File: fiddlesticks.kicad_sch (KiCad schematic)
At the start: 57 parts, among them J1 USB_C_Receptacle_USB2.0_16P, J2 Conn_01x04_Pin, J3 Conn_02x04_Counter_Clockwise, J4 Conn_01x04_Socket, M1 Motor_DC, M2 Motor_DC, M3 Motor_DC, M4 Motor_DC, Q1 AO3400A, Q2 AO3400A, Q3 AO3400A, Q4 AO3400A, SW1 SW_Push, SW2 SW_SPDT, U1 STM32F411CEUx, U2 USBLC6-2SC6, U3 ICM-45605, U4 SPX3819M5-L-3-3, Y1 8MHz 18pF

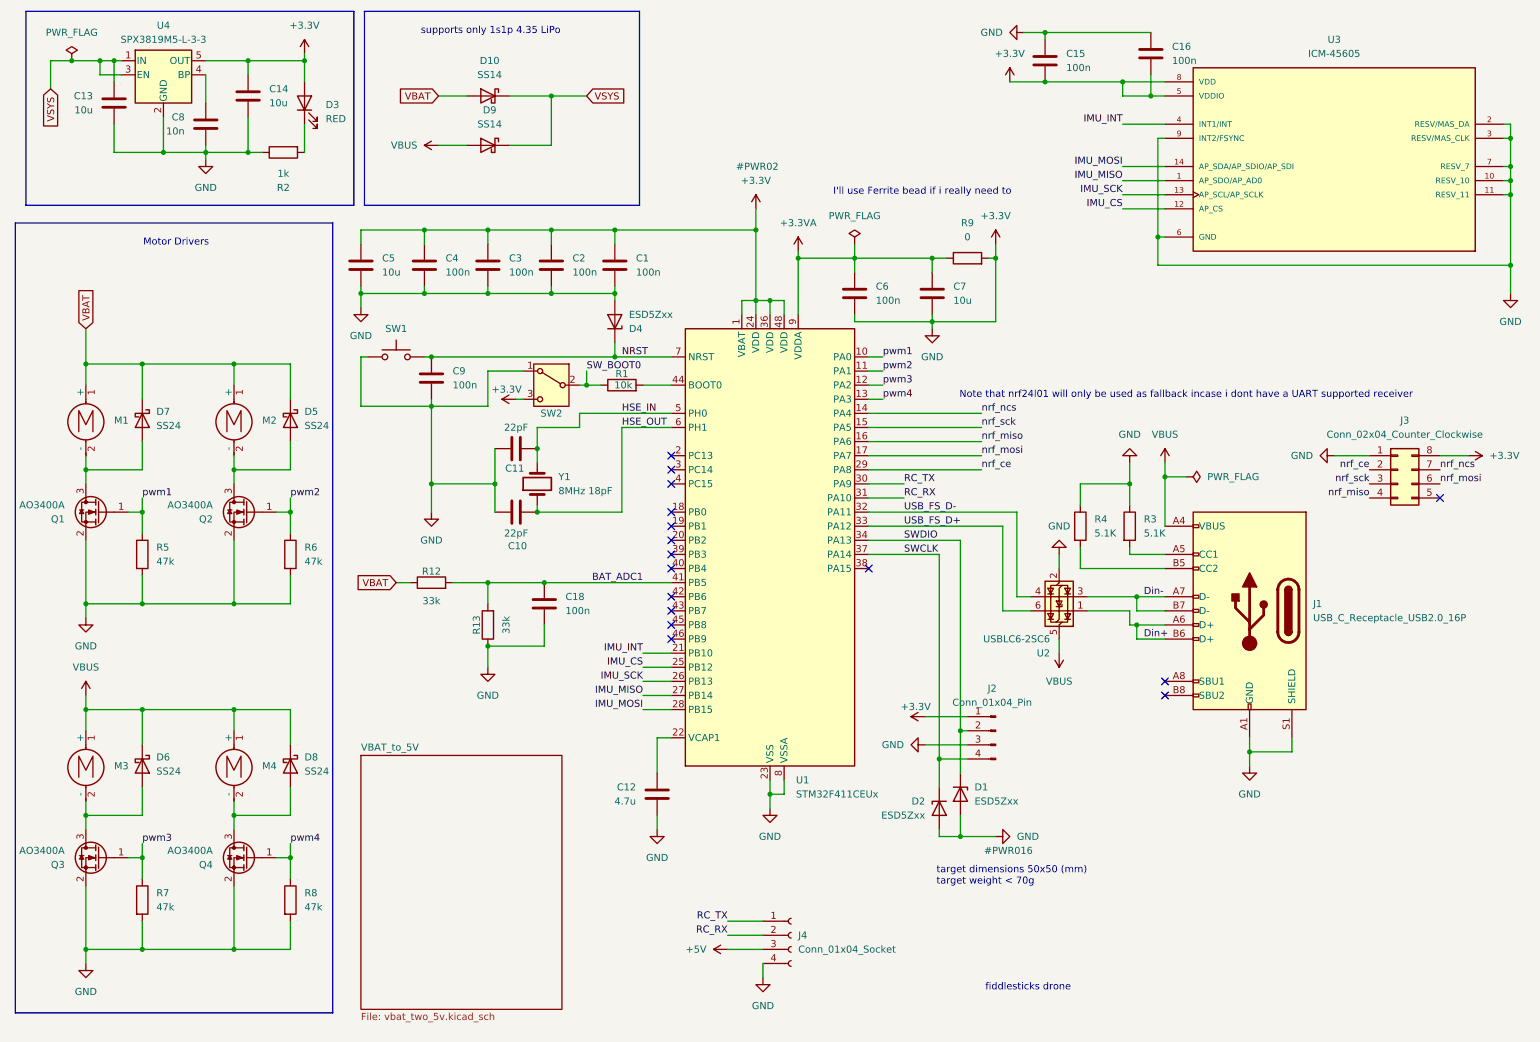
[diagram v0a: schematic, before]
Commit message: changed diodes for power ORing
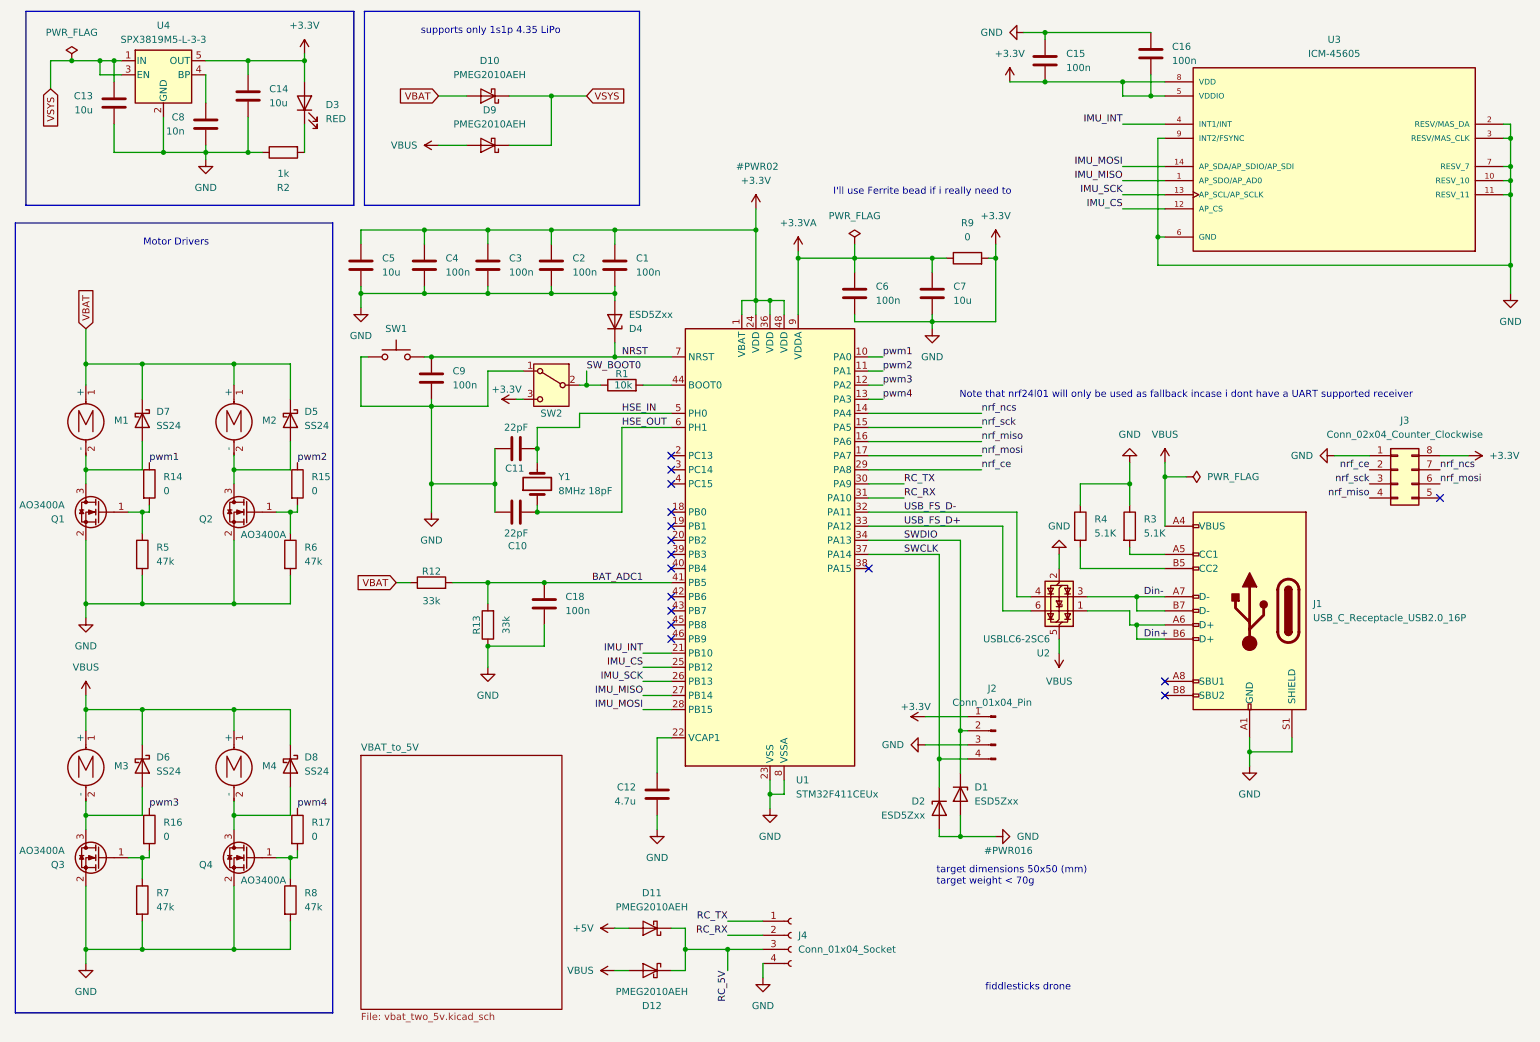
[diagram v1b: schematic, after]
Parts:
- removed D10, D9: SS14, Diode_SMD:D_SMA, symbol Diode:SS14
- added D10, D11, D12, D9: PMEG2010AEH, Diode_SMD:D_SOD-123F, symbol Diode:PMEG2010AEH
- added R14, R15, R16, R17: 0, symbol Device:R
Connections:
- net +5V: now also D11.2 (A); no longer J4.3 (Pin_3)
- net VBAT: now also D10.2 (A)
- net VBUS: now also D12.2 (A), D9.2 (A)
- net VSYS: now also D10.1 (K), D9.1 (K)
- net pwm1: now also R14.1; no longer Q1.1 (G), R5.1
- net pwm2: now also R15.1; no longer Q2.1 (G), R6.1
- net pwm3: now also R16.1; no longer Q3.1 (G), R7.1
- net pwm4: now also R17.1; no longer Q4.1 (G), R8.1
- new net: Q3.1 (G), R16.2, R7.1
- new net: Q1.1 (G), R14.2, R5.1
- new net: Q2.1 (G), R15.2, R6.1
- new net: Q4.1 (G), R17.2, R8.1
- new net RC_5V: D11.1 (K), D12.1 (K), J4.3 (Pin_3)

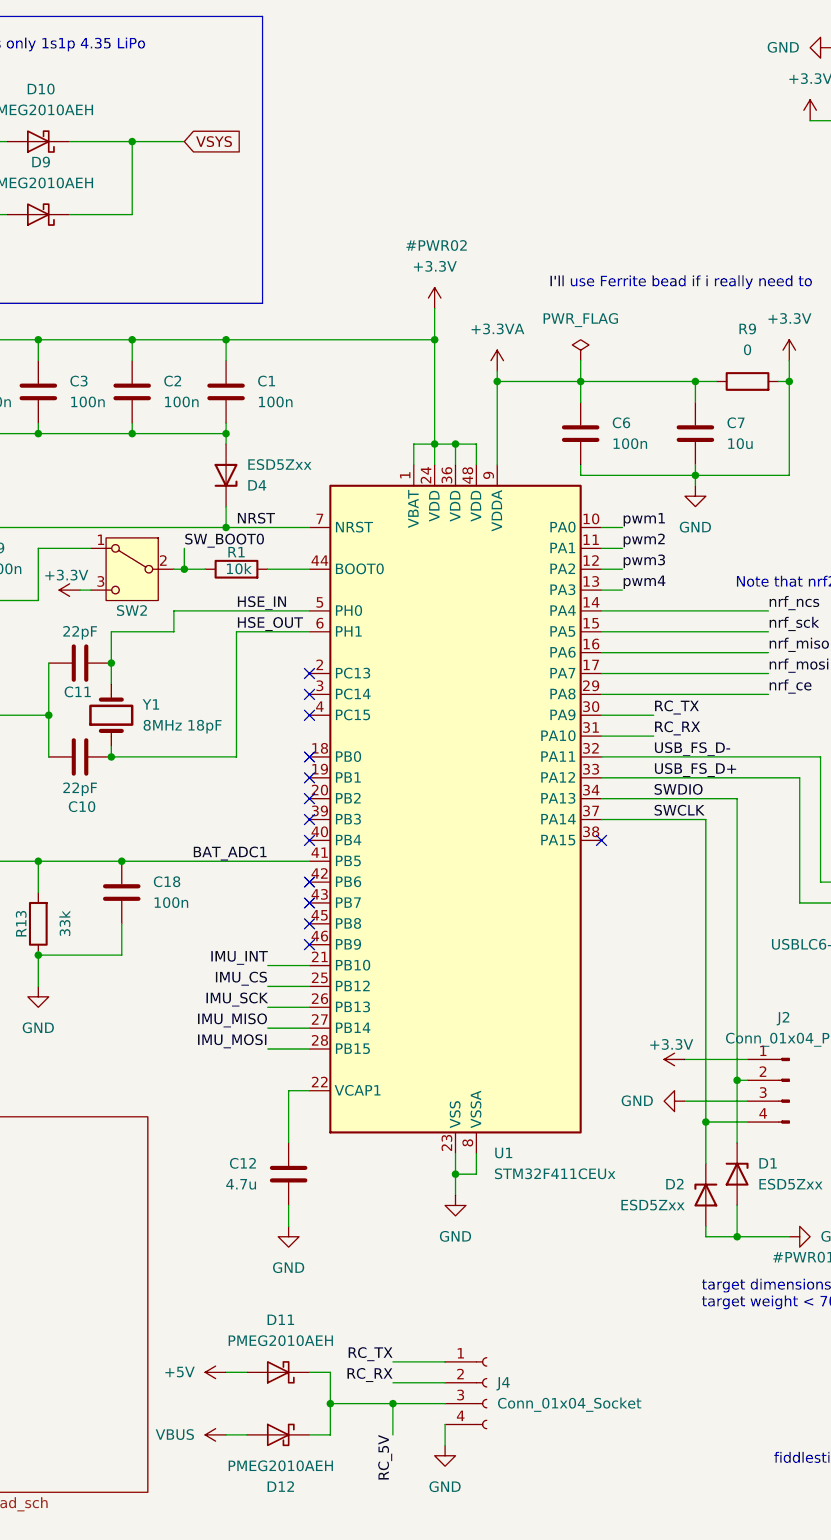
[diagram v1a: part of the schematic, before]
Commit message: added battery connector
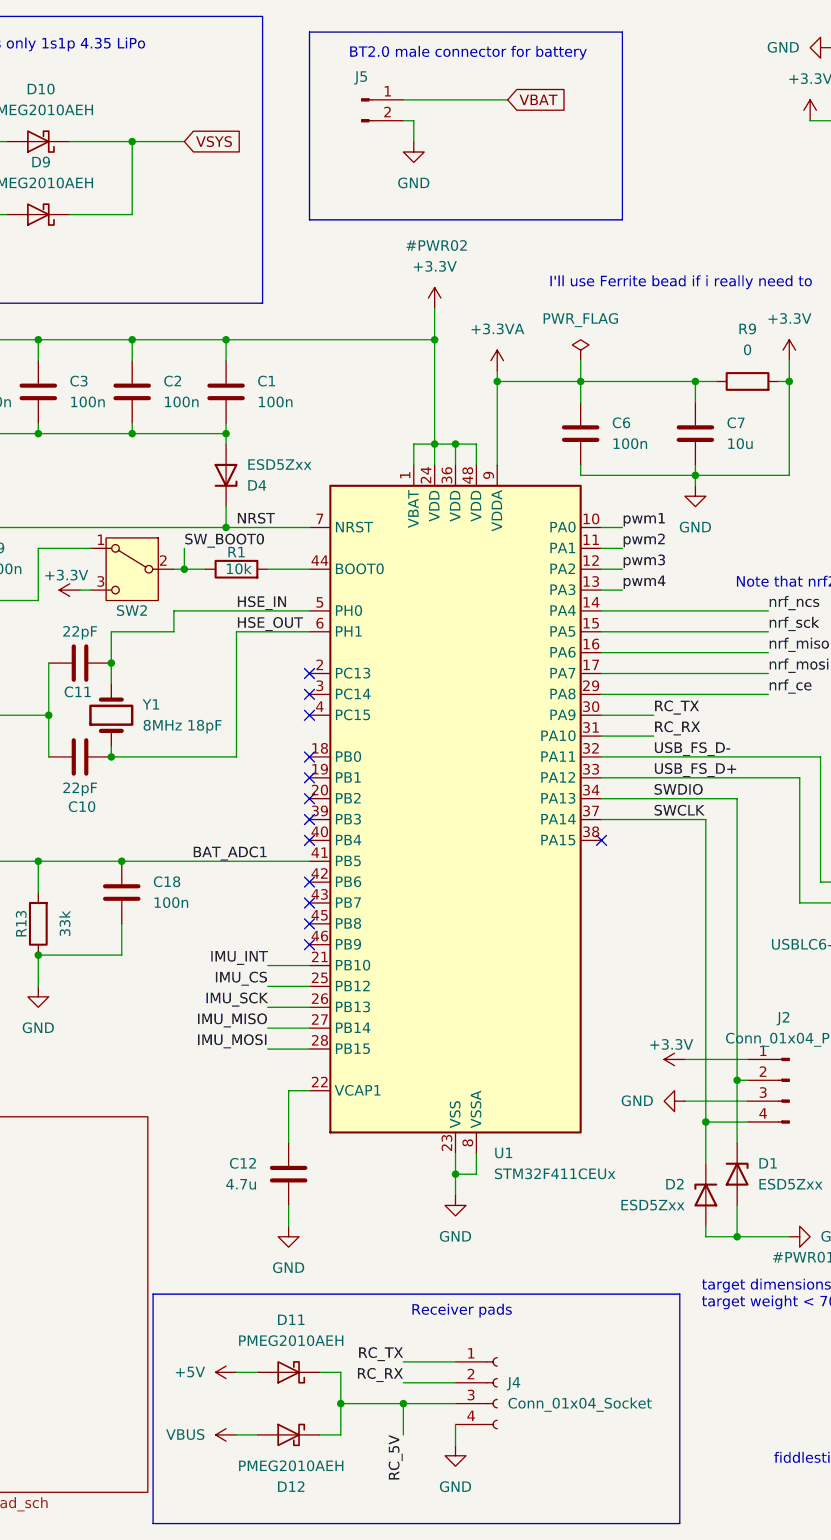
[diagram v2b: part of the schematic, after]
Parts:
- added J5: Conn_01x02_Pin, symbol Connector:Conn_01x02_Pin
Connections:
- net +3.3V: now also J5.2 (Pin_2)
- net VBAT: now also J5.1 (Pin_1)
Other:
- note added: "BT2.0 male connector for battery"
- note added: "Receiver pads"
- moved on the sheet: D11, D12, J4

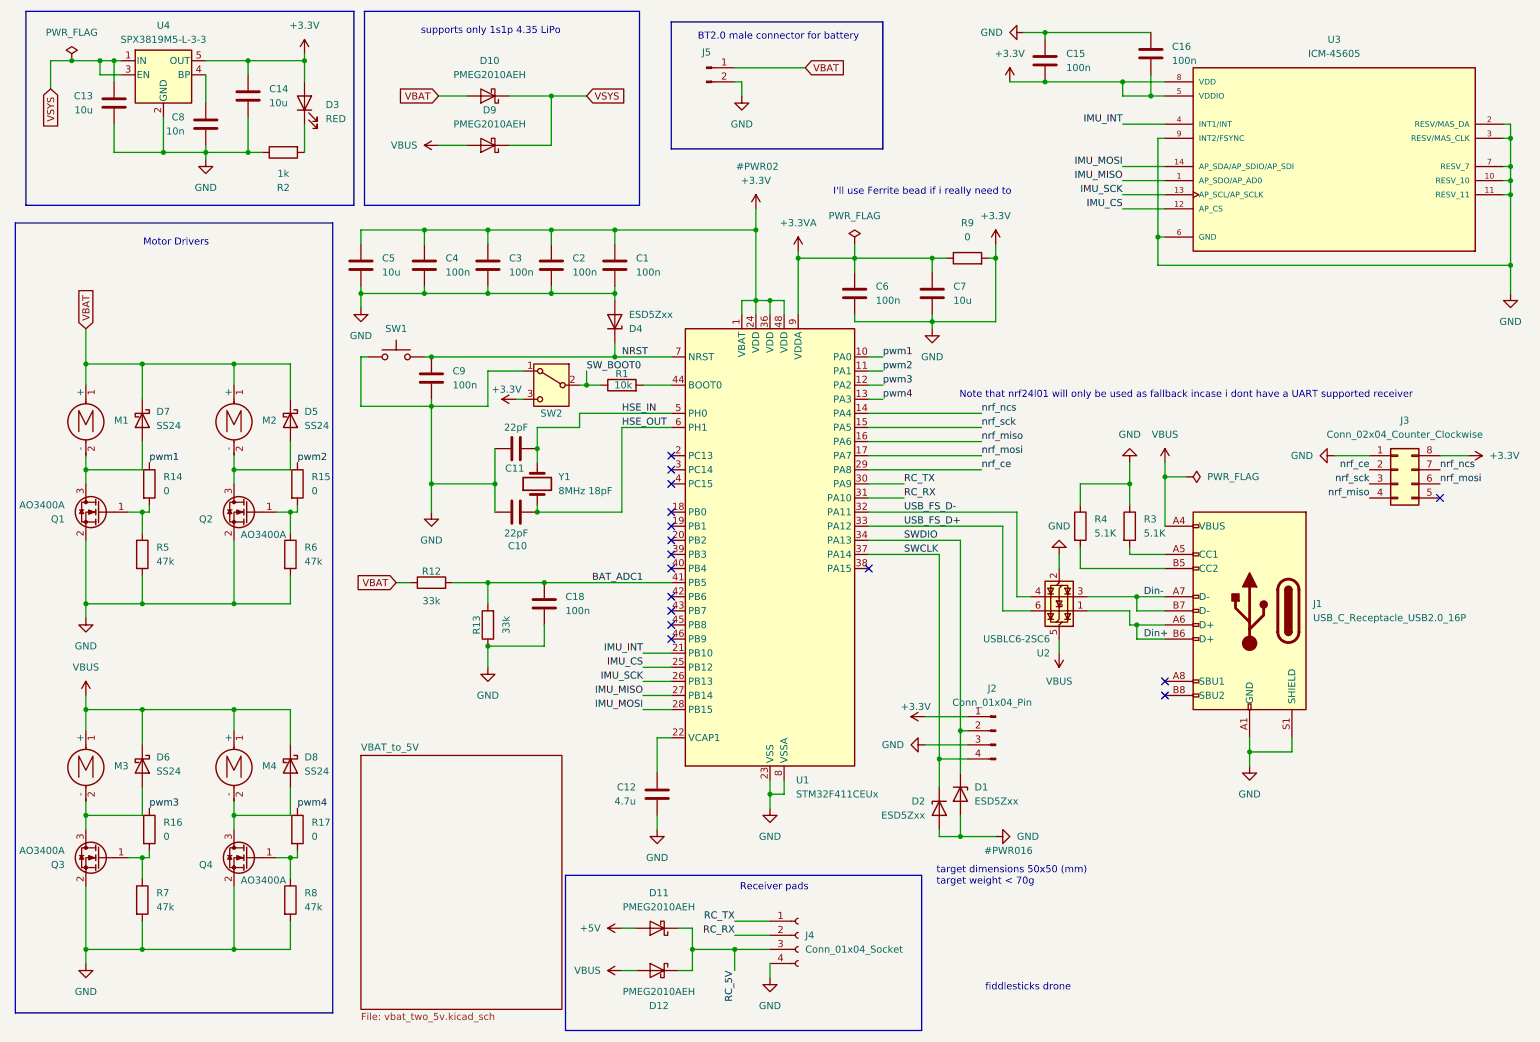
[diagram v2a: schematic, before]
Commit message: assigned footprints
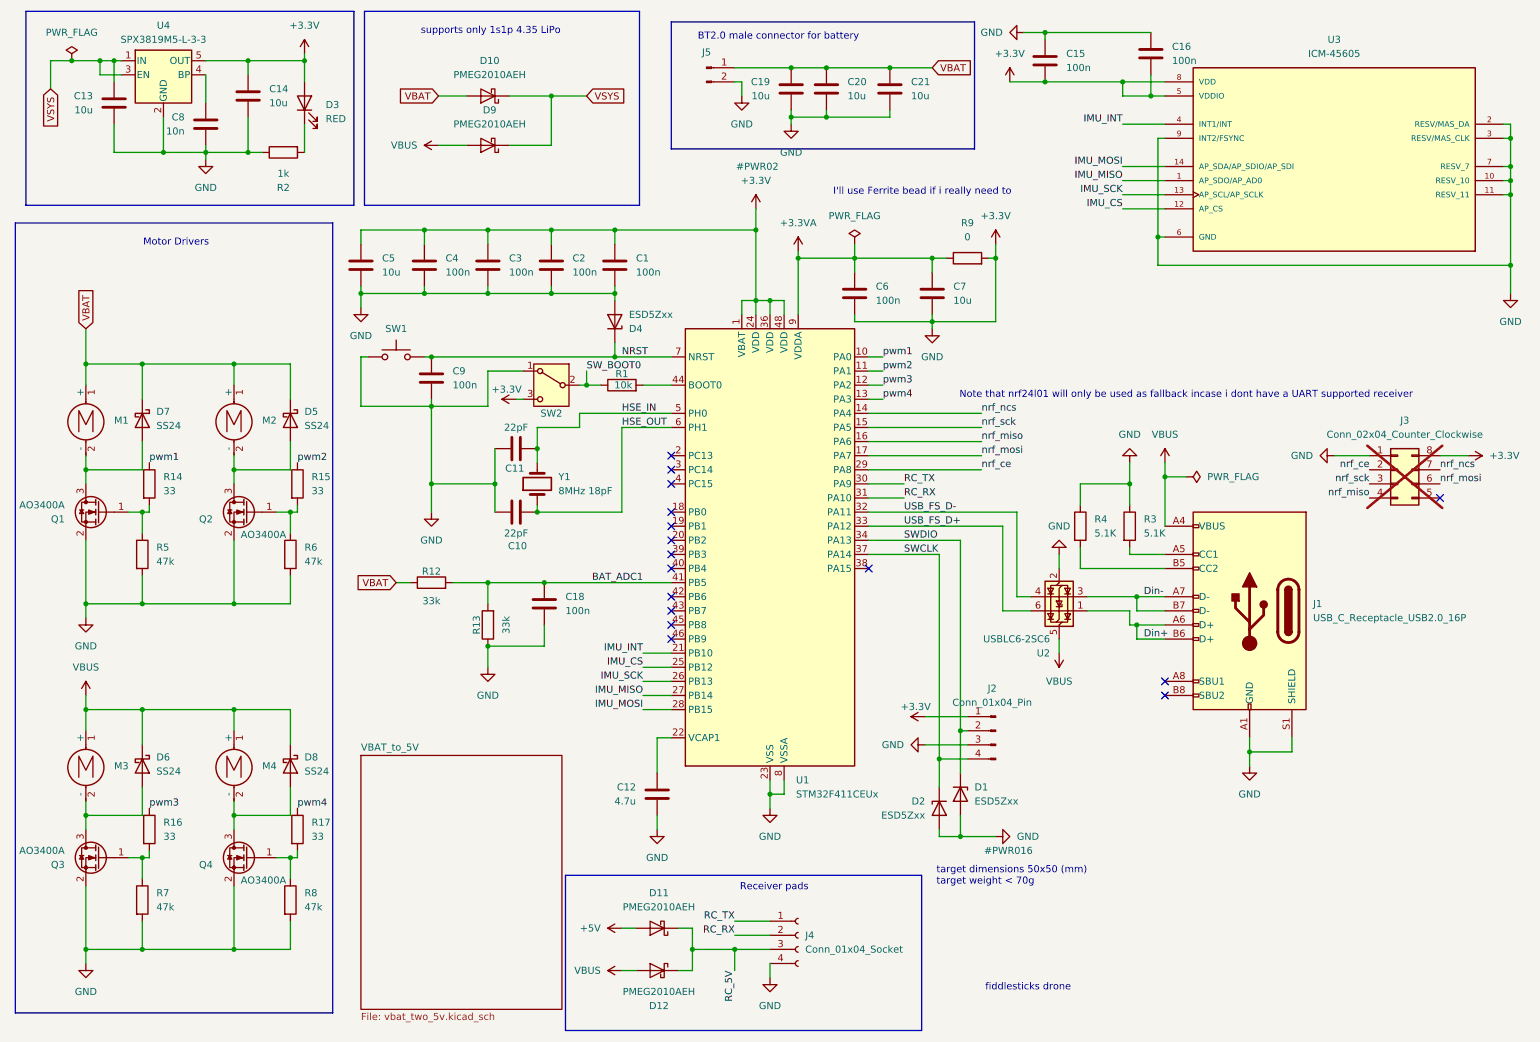
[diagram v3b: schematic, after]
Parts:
- added C19, C20, C21: 10u, Capacitor_SMD:C_0805_2012Metric_Pad1.18x1.45mm_HandSolder, symbol Device:C
- C1, C15, C16, C18, C2, C3, C4, C6, C8, C9: footprint (none) -> Capacitor_SMD:C_0603_1608Metric_Pad1.08x0.95mm_HandSolder
- C12, C13, C14, C5, C7: footprint (none) -> Capacitor_SMD:C_0805_2012Metric_Pad1.18x1.45mm_HandSolder
- D3: footprint (none) -> LED_SMD:LED_0805_2012Metric_Pad1.15x1.40mm_HandSolder
- J2: footprint (none) -> Connector_PinHeader_2.54mm:PinHeader_1x04_P2.54mm_Horizontal
- J3: footprint (none) -> Connector_PinHeader_2.54mm:PinHeader_2x08_P2.54mm_Vertical; now not fitted
- J4: footprint (none) -> Connector_PinHeader_2.54mm:PinHeader_1x04_P2.54mm_Vertical
- R1, R12, R13, R2, R3, R4, R5, R6, R7, R8, R9: footprint (none) -> Resistor_SMD:R_0805_2012Metric_Pad1.20x1.40mm_HandSolder
- R14, R15, R16, R17: value 0 -> 33; footprint (none) -> Resistor_SMD:R_0805_2012Metric_Pad1.20x1.40mm_HandSolder
- U3: footprint ICM-45605:XDCR_ICM-45605 -> IMU:XDCR_ICM-45605
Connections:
- net +3.3V: now also C19.2, C20.2, C21.2
- net VBAT: now also C19.1, C20.1, C21.1
